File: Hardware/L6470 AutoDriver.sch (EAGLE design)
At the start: 35 parts, among them U1 L6470

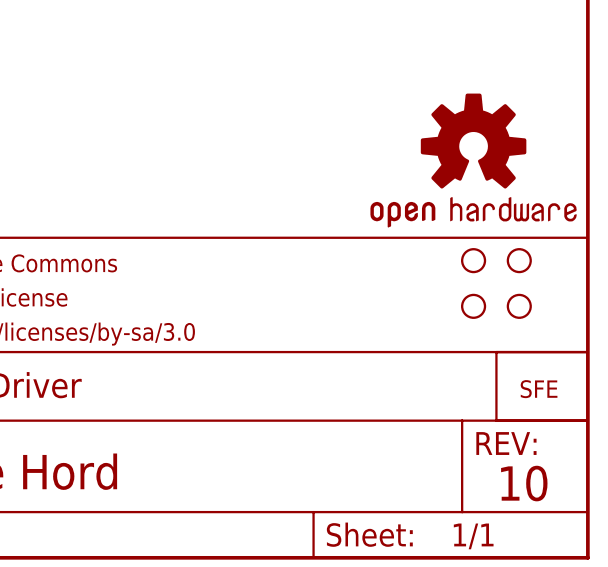
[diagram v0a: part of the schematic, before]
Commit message: Production ready
created 4 board panel; added fiducials
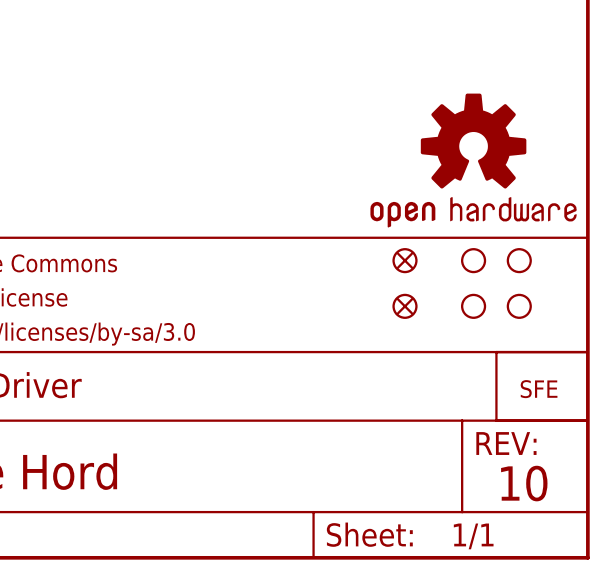
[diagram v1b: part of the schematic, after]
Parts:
- added FID1, FID2: FIDUCIALUFIDUCIAL, SparkFun-Aesthetics:FIDUCIALUFIDUCIAL
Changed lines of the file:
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@@
 <part name="SJ2" library="SparkFun-Passives" deviceset="2PT_GND_TIE" device=""/>
 <part name="U$4" library="SparkFun-Aesthetics" deviceset="FOUR_LAYER_WARNING" device=""/>
+<part name="FID1" library="SparkFun-Aesthetics" deviceset="FIDUCIAL" device="UFIDUCIAL"/>
+<part name="FID2" library="SparkFun-Aesthetics" deviceset="FIDUCIAL" device="UFIDUCIAL"/>
 </parts>
 <sheets>
@@
 <instance part="SJ2" gate="G$1" x="114.3" y="60.96"/>
 <instance part="U$4" gate="G$1" x="147.32" y="36.068"/>
+<instance part="FID1" gate="G$1" x="228.6" y="33.02"/>
+<instance part="FID2" gate="G$1" x="228.6" y="27.94"/>
 </instances>
 <busses>

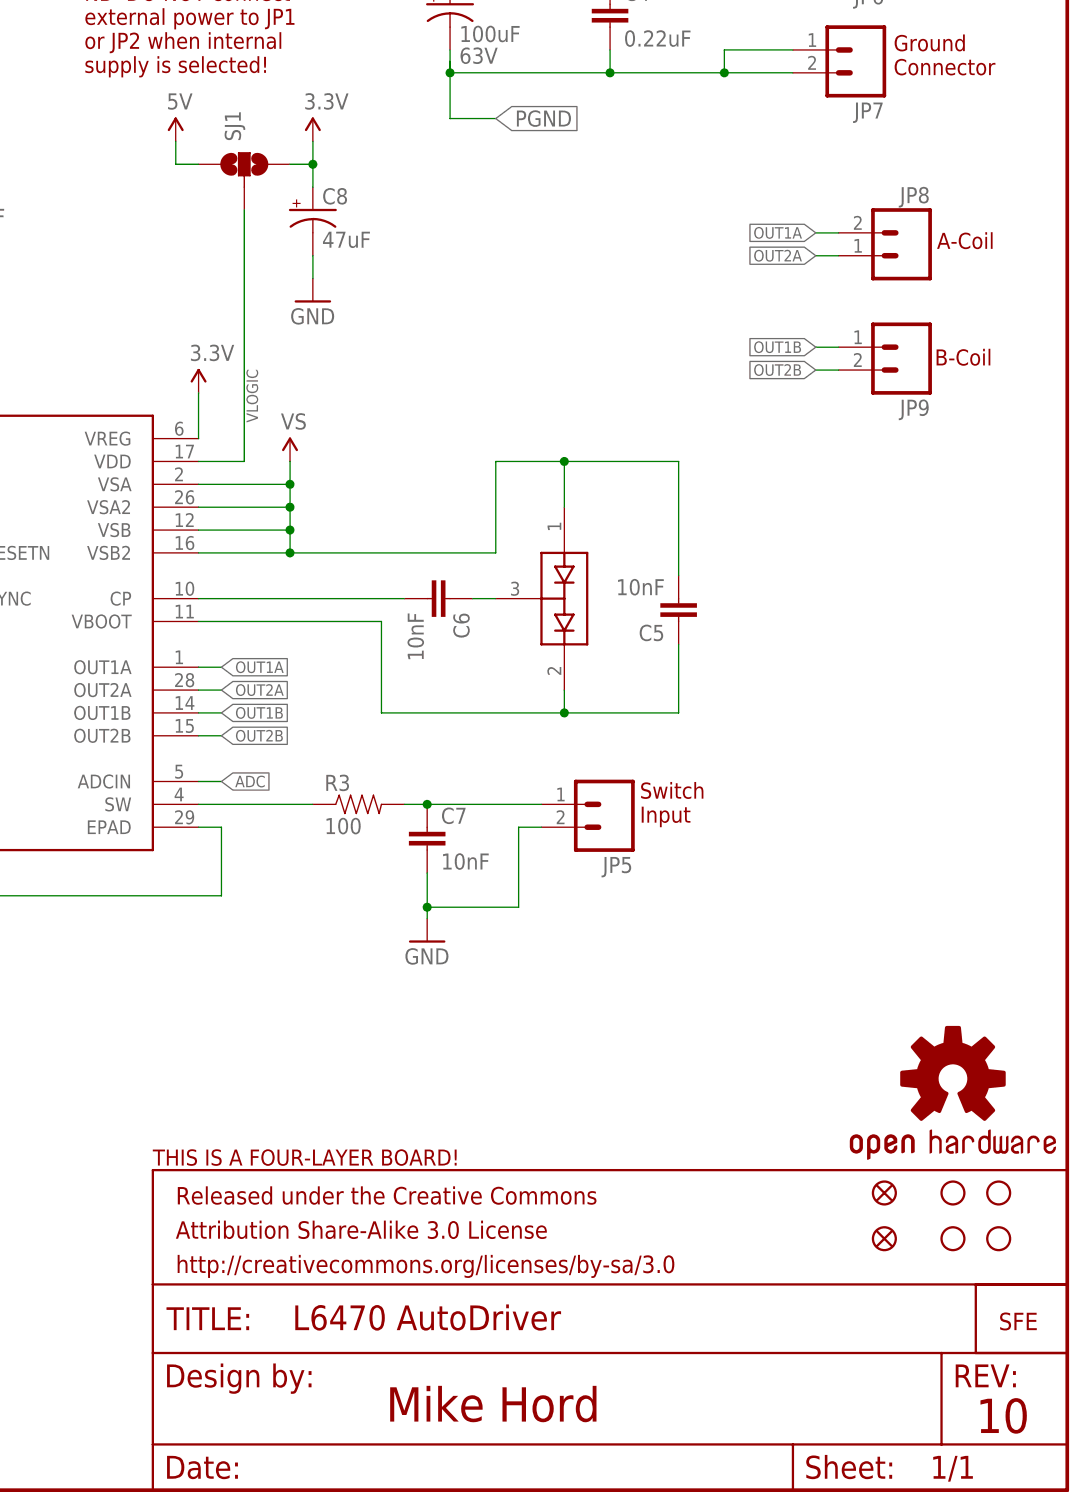
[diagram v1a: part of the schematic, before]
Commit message: 0603 update, Sch work, cap change
Updated res/caps to 0603
large cap updated to smaller silk/pad size
jumper indicator added, OSHW logo upgraded
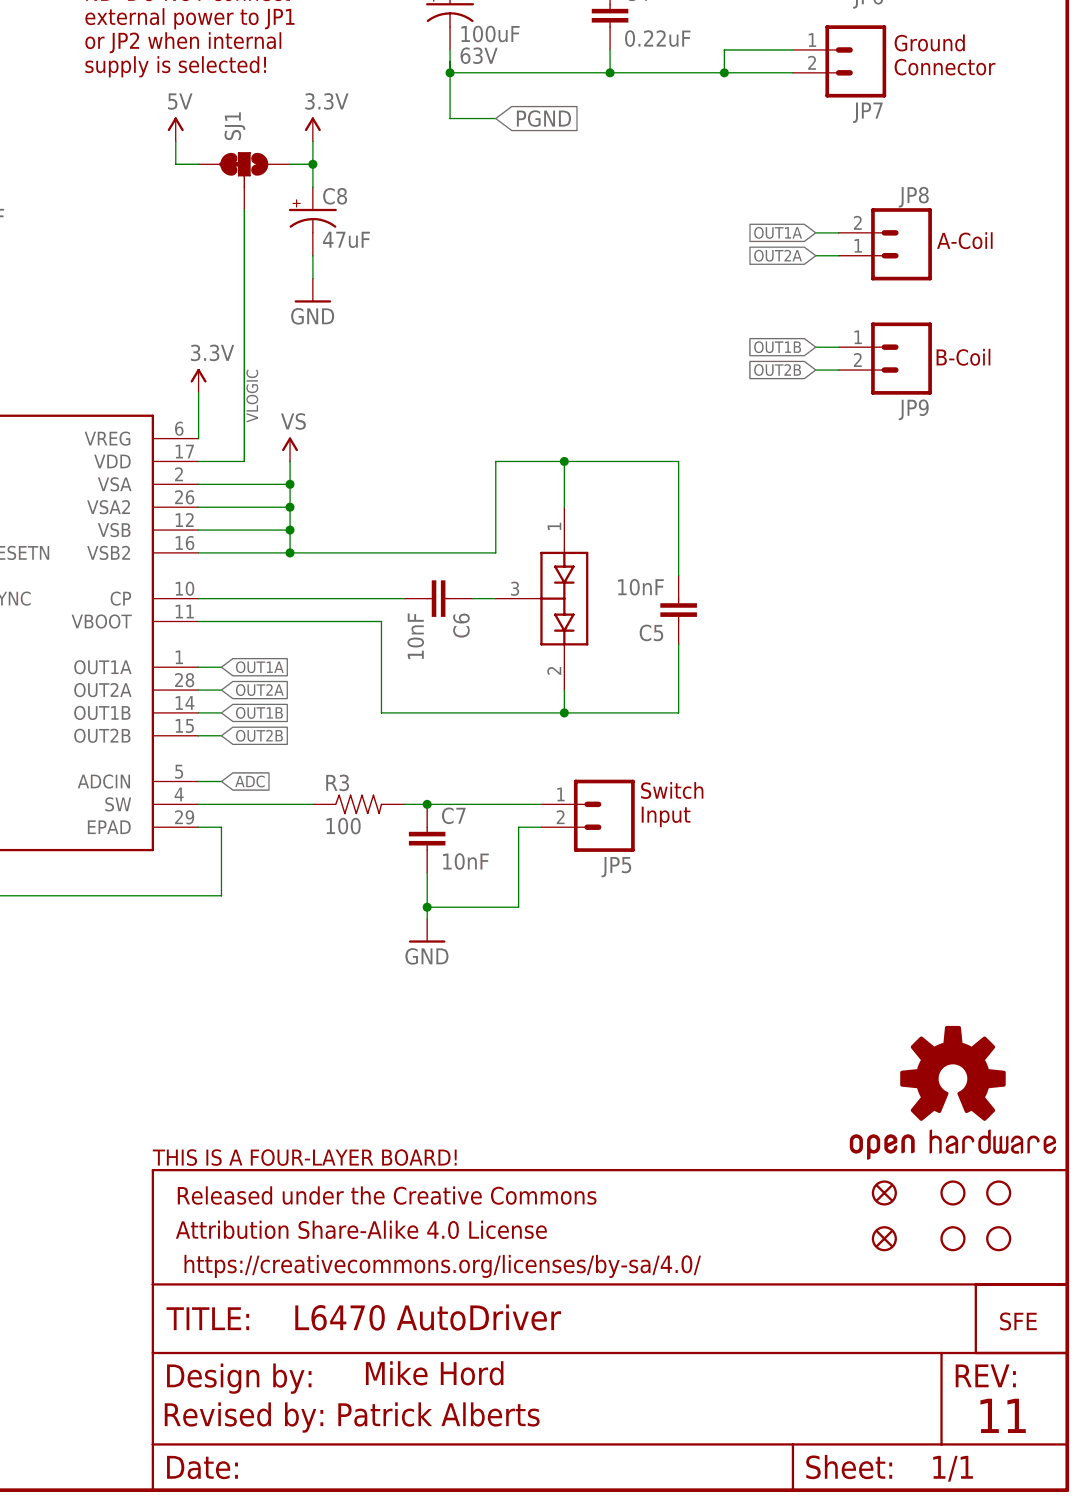
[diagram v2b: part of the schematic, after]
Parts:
- C1: device SparkFun-Capacitors:.1UF-CER -> SparkFun-Capacitors:0.1UF-25V(+80/-20%)(0603)
- C3: device SparkFun-Capacitors:100UF-ELECT -> SparkFun-Capacitors:CAP_POLD
- C4: device SparkFun-Capacitors:.22UF-CER -> SparkFun-Capacitors:0.22UF50V-20%,+80%(0603)
- C5, C6, C7: device SparkFun-Capacitors:10NF-CER -> SparkFun-Capacitors:10NF/10000PF-50V-10%(0603)
- LOGO1: value OSHW-LOGOS -> OSHW-LOGOM; device SparkFun:OSHW-LOGOS -> SparkFun-Aesthetics:OSHW-LOGOM
- R1, R2: device SparkFun-Resistors:10K-1%RES-00824 -> SparkFun-Resistors:10KOHM1/10W1%(0603)0603
- R3: device SparkFun-Resistors:100-1% -> SparkFun-Resistors:100OHM1/10W1%(0603)
- R5: device SparkFun-Resistors:8.2K-5% -> SparkFun-Resistors:8.2KOHM-1/10W-5%(0603)
- R6: device SparkFun-Resistors:33K-1% -> SparkFun-Resistors:33KOHM1/10W1%(0603)
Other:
- note added: "11"
- note added: "Revised by: Patrick Alberts"
- note removed: "10"
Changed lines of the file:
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@@
 <layer number="106" name="bPlate" color="7" fill="1" visible="no" active="yes"/>
 <layer number="107" name="Crop" color="7" fill="1" visible="no" active="yes"/>
+<layer number="108" name="tplace-old" color="10" fill="1" visible="no" active="yes"/>
+<layer number="109" name="ref-old" color="11" fill="1" visible="no" active="yes"/>
 <layer number="116" name="Patch_BOT" color="9" fill="4" visible="no" active="yes"/>
 <layer number="121" name="_tsilk" color="7" fill="1" visible="no" active="yes"/>
@@
 <part name="JP2" library="SparkFun-Connectors" deviceset="M05X2" device="SHD"/>
 <part name="GND2" library="SparkFun" deviceset="GND" device=""/>
-<part name="C1" library="SparkFun-Capacitors" deviceset=".1UF-CER" device="" value="0.1uF"/>
-<part name="R1" library="SparkFun-Resistors" deviceset="10K-1%" device="RES-00824" value="10k"/>
-<part name="R2" library="SparkFun-Resistors" deviceset="10K-1%" device="RES-00824" value="10k"/>
+<part name="C1" library="SparkFun-Capacitors" deviceset="0.1UF-25V(+80/-20%)(0603)" device="" value="0.1uF"/>
+<part name="R1" library="SparkFun-Resistors" deviceset="10KOHM1/10W1%(0603)" device="0603" value="10k"/>
+<part name="R2" library="SparkFun-Resistors" deviceset="10KOHM1/10W1%(0603)" device="0603" value="10k"/>
 <part name="GND3" library="SparkFun" deviceset="GND" device=""/>
 <part name="LOGO2" library="SparkFun" deviceset="LOGO-SFE" device="NEW"/>
@@
 <part name="GND6" library="SparkFun" deviceset="GND" device=""/>
 <part name="D1" library="SparkFun-DiscreteSemi" deviceset="BAV99" device="" value="BAV99"/>
-<part name="C6" library="SparkFun-Capacitors" deviceset="10NF-CER" device="" value="10nF"/>
-<part name="C5" library="SparkFun-Capacitors" deviceset="10NF-CER" device="" value="10nF"/>
-<part name="C4" library="SparkFun-Capacitors" deviceset=".22UF-CER" device="" value="0.22uF"/>
-<part name="C3" library="SparkFun-Capacitors" deviceset="100UF-ELECT" device="" value="100uF"/>
+<part name="C6" library="SparkFun-Capacitors" deviceset="10NF/10000PF-50V-10%(0603)" device="" value="10nF"/>
+<part name="C5" library="SparkFun-Capacitors" deviceset="10NF/10000PF-50V-10%(0603)" device="" value="10nF"/>
+<part name="C4" library="SparkFun-Capacitors" deviceset="0.22UF50V-20%,+80%(0603)" device="" value="0.22uF"/>
+<part name="C3" library="SparkFun-Capacitors" deviceset="CAP_POL" device="D" value="100uF"/>
 <part name="P+2" library="SparkFun" deviceset="VCC" device="" value="VS"/>
 <part name="JP7" library="SparkFun" deviceset="M02" device="3.5MM"/>
@@
 <part name="JP9" library="SparkFun" deviceset="M02" device="3.5MM"/>
 <part name="JP5" library="SparkFun" deviceset="M02" device="3.5MM"/>
-<part name="C7" library="SparkFun-Capacitors" deviceset="10NF-CER" device="" value="10nF"/>
-<part name="R3" library="SparkFun-Resistors" deviceset="100-1%" device="" value="100"/>
+<part name="C7" library="SparkFun-Capacitors" deviceset="10NF/10000PF-50V-10%(0603)" device="" value="10nF"/>
+<part name="R3" library="SparkFun-Resistors" deviceset="100OHM1/10W1%(0603)" device="" value="100"/>
 <part name="GND7" library="SparkFun" deviceset="GND" device=""/>
 <part name="R4" library="SparkFun" deviceset="POT" device="100K_3362U" value="200k"/>
-<part name="R5" library="SparkFun-Resistors" deviceset="8.2K-5%" device="" value="8.2k"/>
-<part name="R6" library="SparkFun-Resistors" deviceset="33K-1%" device="" value="33k"/>
+<part name="R5" library="SparkFun-Resistors" deviceset="8.2KOHM-1/10W-5%(0603)" device="" value="8.2k"/>
+<part name="R6" library="SparkFun-Resistors" deviceset="33KOHM1/10W1%(0603)" device="" value="33k"/>
 <part name="P+3" library="SparkFun" deviceset="VCC" device="" value="VS"/>
 <part name="GND8" library="SparkFun" deviceset="GND" device=""/>
@@
 <part name="STANDOFF1" library="SparkFun" deviceset="STAND-OFF" device=""/>
 <part name="STANDOFF3" library="SparkFun" deviceset="STAND-OFF" device=""/>
-<part name="LOGO1" library="SparkFun" deviceset="OSHW-LOGO" device="S"/>
+<part name="LOGO1" library="SparkFun-Aesthetics" deviceset="OSHW-LOGO" device="M"/>
 <part name="FRAME1" library="SparkFun-Aesthetics" deviceset="FRAME-LETTER" device=""/>
 <part name="SJ1" library="SparkFun-Passives" deviceset="SOLDERJUMPER_2WAY" device="PASTE1&amp;2"/>
@@
 <sheet>
 <plain>
-<text x="173.228" y="7.62" size="3.81" layer="94">Mike Hord</text>
-<text x="238.76" y="6.35" size="3.81" layer="94">10</text>
+<text x="170.688" y="11.684" size="2.54" layer="94">Mike Hord</text>
+<text x="238.76" y="6.35" size="3.81" layer="94">11</text>
 <text x="181.356" y="158.496" size="1.778" layer="96">63V</text>
 <text x="201.422" y="74.168" size="1.778" layer="94">Switch
@@
 CPOL=CPHA=1
 5 Mbit max</text>
+<text x="148.336" y="7.112" size="2.54" layer="94">Revised by: Patrick Alberts</text>
+<wire x1="157.48" y1="147.32" x2="154.94" y2="147.32" width="0.508" layer="94"/>
 </plain>
 <instances>

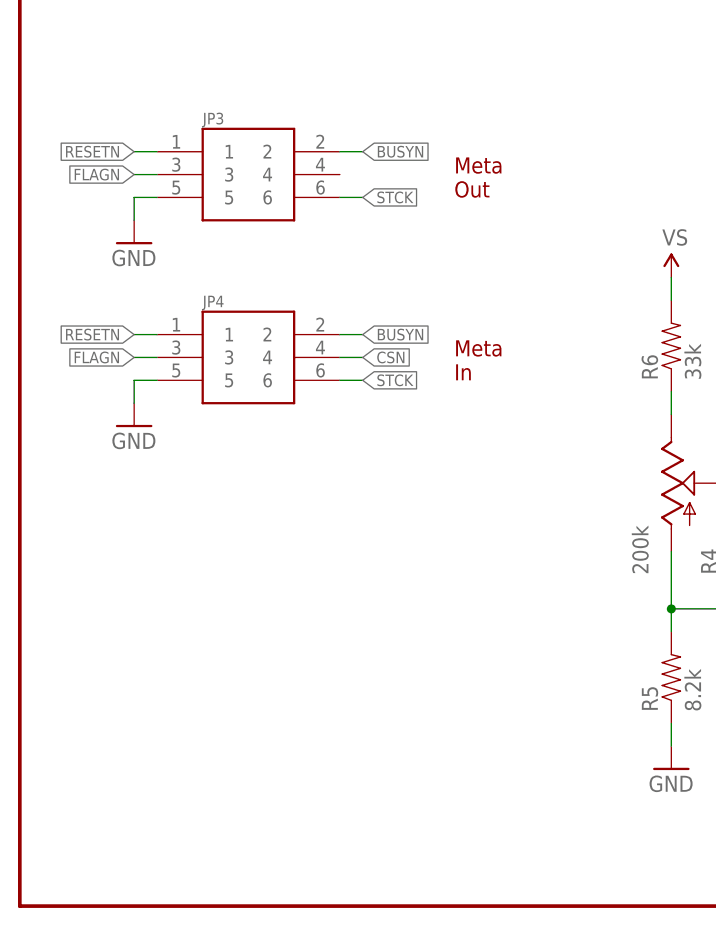
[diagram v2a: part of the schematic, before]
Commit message: Connect CSN to CSN_OUT, minor fixes
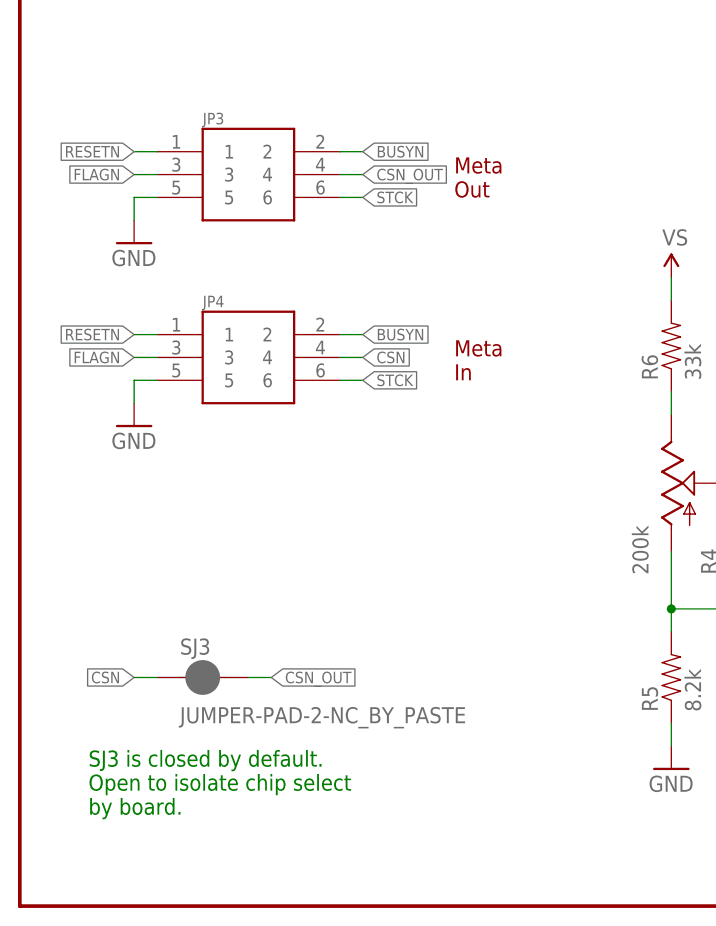
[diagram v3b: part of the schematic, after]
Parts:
- added SJ3: JUMPER-PAD-2-NC_BY_PASTE, SparkFun-Passives:JUMPER-PAD-2-NC_BY_PASTE
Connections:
- new net CSN_OUT: JP3.4, SJ3.2
- net CSN: now also SJ3.1
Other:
- note added: "SJ3 is closed by default. Open to isolate chip select by board."
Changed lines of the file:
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@@
 <?xml version="1.0" encoding="utf-8"?>
 <!DOCTYPE eagle SYSTEM "eagle.dtd">
-<eagle version="6.4">
+<eagle version="6.5.0">
 <drawing>
 <settings>
@@
 <layer number="254" name="cooling" color="7" fill="1" visible="no" active="yes"/>
 </layers>
-<schematic xreflabel="%F%N/%S.%C%R" xrefpart="/%S.%C%R">
+<schematic xreflabel="%F%N/%S" xrefpart="1_/%S.%C%R">
 <attributes>
 </attributes>
@@
 <part name="FID1" library="SparkFun-Aesthetics" deviceset="FIDUCIAL" device="UFIDUCIAL"/>
 <part name="FID2" library="SparkFun-Aesthetics" deviceset="FIDUCIAL" device="UFIDUCIAL"/>
+<part name="SJ3" library="SparkFun-Passives" deviceset="JUMPER-PAD-2-NC_BY_PASTE" device=""/>
 </parts>
 <sheets>
@@
 <text x="148.336" y="7.112" size="2.54" layer="94">Revised by: Patrick Alberts</text>
 <wire x1="157.48" y1="147.32" x2="154.94" y2="147.32" width="0.508" layer="94"/>
+<text x="7.62" y="10.16" size="1.778" layer="91">SJ3 is closed by default.
+Open to isolate chip select
+by board.</text>
 </plain>
 <instances>
@@
 <instance part="FID1" gate="G$1" x="228.6" y="33.02"/>
 <instance part="FID2" gate="G$1" x="228.6" y="27.94"/>
+<instance part="SJ3" gate="G$1" x="20.32" y="25.4"/>
 </instances>
 <busses>
@@
 <wire x1="35.56" y1="60.96" x2="38.1" y2="60.96" width="0.1524" layer="91"/>
 <label x="38.1" y="60.96" size="1.27" layer="95" xref="yes"/>
+</segment>
+<segment>
+<pinref part="SJ3" gate="G$1" pin="1"/>
+<wire x1="15.24" y1="25.4" x2="12.7" y2="25.4" width="0.1524" layer="91"/>
+<label x="12.7" y="25.4" size="1.27" layer="95" rot="R180" xref="yes"/>
 </segment>
 </net>
@@
 </segment>
 </net>
+<net name="CSN_OUT" class="0">
+<segment>
+<pinref part="JP3" gate="G$1" pin="4"/>
+<wire x1="35.56" y1="81.28" x2="38.1" y2="81.28" width="0.1524" layer="91"/>
+<label x="38.1" y="81.28" size="1.27" layer="95" xref="yes"/>
+</segment>
+<segment>
+<pinref part="SJ3" gate="G$1" pin="2"/>
+<wire x1="25.4" y1="25.4" x2="27.94" y2="25.4" width="0.1524" layer="91"/>
+<label x="27.94" y="25.4" size="1.27" layer="95" xref="yes"/>
+</segment>
+</net>
